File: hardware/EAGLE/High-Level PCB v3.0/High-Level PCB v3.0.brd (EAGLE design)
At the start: 100 x 80 mm, 58 parts, among them IC1 MCP2551, IC2 DS8921, IC3 DS8921, J1 Micro-SD, J2 Optical Mouse, J3 Gyro, J4 DB9 Plug, J5 CAN Output, J6 RaspπUart, U1 GPS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

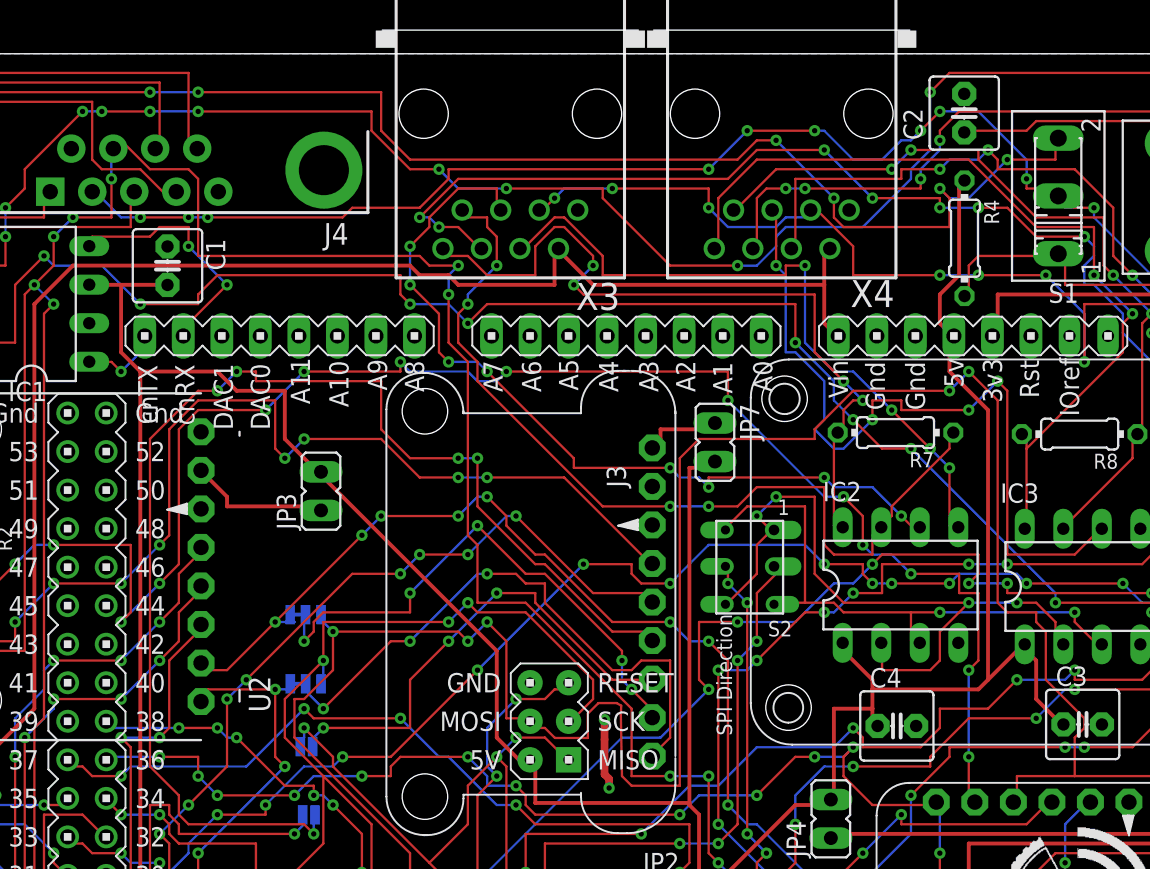
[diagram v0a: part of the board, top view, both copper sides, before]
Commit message: Fixed Click signal and made new gerbers
Click signals from the low level systems are now tied together.
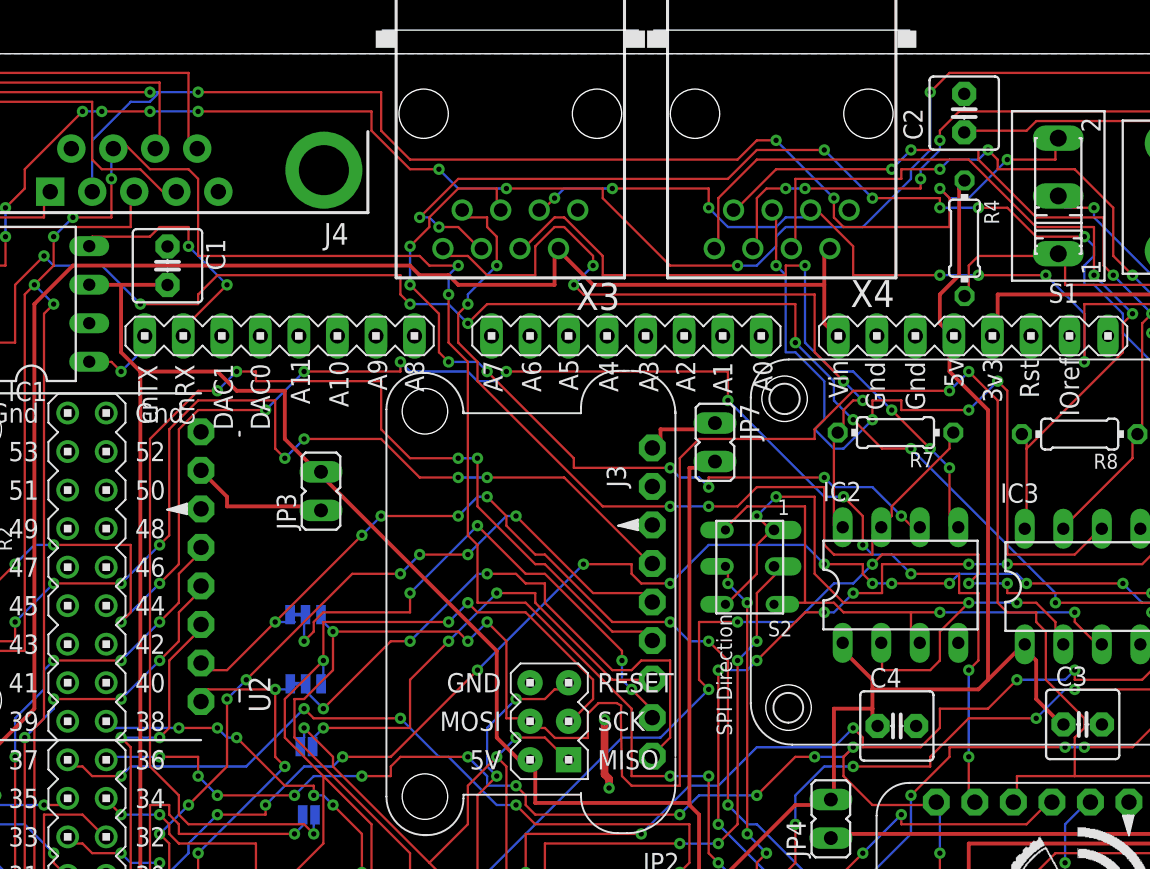
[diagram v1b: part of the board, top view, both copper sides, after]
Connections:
- removed net N$6: S1.3, X2.21
- new net CLICK_LL: J4.4, S1.3, X2.21
- net CLICK: no longer J4.4
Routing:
- net CLICK_LL: track 0.00 -> 166.7 mm, vias 0 -> 10
- net N$6: track 157.5 -> 0.00 mm, vias 10 -> 0
- net CLICK: track 164.8 -> 92.0 mm, vias 17 -> 8
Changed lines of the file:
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@@
 <via x="56.3" y="31.6" extent="1-16" drill="0.35"/>
 <via x="56" y="36.1" extent="1-16" drill="0.35"/>
-<wire x1="56" y1="32.5" x2="56" y2="34.8" width="0.508" layer="1"/>
-<wire x1="56" y1="34.8" x2="56" y2="36.1" width="0.508" layer="1"/>
+<wire x1="56" y1="32.5" x2="56" y2="36.1" width="0.508" layer="1"/>
 <wire x1="56.3" y1="31.6" x2="56.3" y2="32.2" width="0.508" layer="1"/>
 <wire x1="56.3" y1="32.2" x2="56" y2="32.5" width="0.508" layer="1"/>
@@
 <contactref element="S1" pad="2"/>
 <contactref element="U3" pad="17"/>
-<contactref element="J4" pad="4"/>
-<wire x1="83.82" y1="71.12" x2="85.725" y2="71.12" width="0.1524" layer="1"/>
-<wire x1="83.82" y1="71.755" x2="83.82" y2="71.12" width="0.1524" layer="1"/>
-<wire x1="83.82" y1="73.025" x2="83.82" y2="71.755" width="0.1524" layer="16"/>
-<wire x1="80.645" y1="76.2" x2="83.82" y2="73.025" width="0.1524" layer="16"/>
-<wire x1="78.105" y1="76.2" x2="80.645" y2="76.2" width="0.1524" layer="16"/>
-<wire x1="76.835" y1="74.93" x2="78.105" y2="76.2" width="0.1524" layer="1"/>
-<wire x1="76.2" y1="74.295" x2="76.835" y2="74.93" width="0.1524" layer="16"/>
-<wire x1="75.565" y1="74.295" x2="76.2" y2="74.295" width="0.1524" layer="16"/>
-<wire x1="74.295" y1="73.025" x2="75.565" y2="74.295" width="0.1524" layer="16"/>
-<wire x1="72.39" y1="73.025" x2="74.295" y2="73.025" width="0.1524" layer="16"/>
-<wire x1="70.485" y1="74.93" x2="72.39" y2="73.025" width="0.1524" layer="16"/>
-<wire x1="69.85" y1="74.93" x2="70.485" y2="74.93" width="0.1524" layer="16"/>
-<wire x1="65.405" y1="74.93" x2="69.85" y2="74.93" width="0.1524" layer="1"/>
-<wire x1="62.865" y1="72.39" x2="65.405" y2="74.93" width="0.1524" layer="16"/>
-<wire x1="45.72" y1="72.39" x2="62.865" y2="72.39" width="0.1524" layer="1"/>
-<wire x1="45.72" y1="71.755" x2="45.72" y2="72.39" width="0.1524" layer="1"/>
-<wire x1="43.815" y1="69.85" x2="45.72" y2="71.755" width="0.1524" layer="1"/>
-<wire x1="39.37" y1="69.85" x2="43.815" y2="69.85" width="0.1524" layer="1"/>
-<wire x1="38.735" y1="69.215" x2="39.37" y2="69.85" width="0.1524" layer="1"/>
-<wire x1="29.845" y1="69.215" x2="38.735" y2="69.215" width="0.1524" layer="1"/>
-<wire x1="28.575" y1="69.215" x2="29.845" y2="69.215" width="0.1524" layer="16"/>
-<wire x1="25.4" y1="69.215" x2="28.575" y2="69.215" width="0.1524" layer="1"/>
-<wire x1="24.13" y1="69.215" x2="25.4" y2="69.215" width="0.1524" layer="16"/>
-<wire x1="22.86" y1="70.485" x2="24.13" y2="69.215" width="0.1524" layer="16"/>
-<wire x1="85.725" y1="71.12" x2="85.91" y2="70.63" width="0.1524" layer="1"/>
-<wire x1="22.86" y1="70.485" x2="22.23" y2="70.91" width="0.1524" layer="16"/>
 <wire x1="64.77" y1="21.59" x2="63.5" y2="20.32" width="0.1524" layer="1"/>
 <wire x1="67.945" y1="21.59" x2="64.77" y2="21.59" width="0.1524" layer="16"/>
@@
 <wire x1="63.5" y1="20.32" x2="63.4" y2="19.86" width="0.1524" layer="1"/>
 <wire x1="86.36" y1="70.485" x2="85.91" y2="70.63" width="0.1524" layer="1"/>
-<via x="83.82" y="71.755" extent="1-16" drill="0.35"/>
-<via x="78.105" y="76.2" extent="1-16" drill="0.35"/>
-<via x="76.835" y="74.93" extent="1-16" drill="0.35"/>
-<via x="69.85" y="74.93" extent="1-16" drill="0.35"/>
-<via x="65.405" y="74.93" extent="1-16" drill="0.35"/>
-<via x="62.865" y="72.39" extent="1-16" drill="0.35"/>
-<via x="29.845" y="69.215" extent="1-16" drill="0.35"/>
-<via x="28.575" y="69.215" extent="1-16" drill="0.35"/>
-<via x="25.4" y="69.215" extent="1-16" drill="0.35"/>
 <via x="64.77" y="21.59" extent="1-16" drill="0.35"/>
 <via x="67.945" y="21.59" extent="1-16" drill="0.35"/>
@@
 <via x="18.415" y="64.77" extent="1-16" drill="0.35"/>
 </signal>
-<signal name="N$6">
+<signal name="CLICK_LL">
 <contactref element="S1" pad="3"/>
 <contactref element="X2" pad="21"/>
@@
 <wire x1="12.7" y1="77.47" x2="11.43" y2="76.2" width="0.1524" layer="1"/>
 <wire x1="26.035" y1="77.47" x2="12.7" y2="77.47" width="0.1524" layer="1"/>
-<wire x1="29.21" y1="77.47" x2="26.035" y2="77.47" width="0.1524" layer="16"/>
+<wire x1="29.21" y1="77.47" x2="26.67" y2="77.47" width="0.1524" layer="16"/>
+<wire x1="26.67" y1="77.47" x2="26.035" y2="77.47" width="0.1524" layer="16"/>
 <wire x1="41.275" y1="77.47" x2="29.21" y2="77.47" width="0.1524" layer="1"/>
 <wire x1="41.275" y1="74.93" x2="41.275" y2="77.47" width="0.1524" layer="1"/>
@@
 <via x="78.105" y="71.12" extent="1-16" drill="0.35"/>
 <via x="82.55" y="73.025" extent="1-16" drill="0.35"/>
+<contactref element="J4" pad="4"/>
+<wire x1="22.225" y1="74.295" x2="22.225" y2="71.12" width="0.1524" layer="16"/>
+<wire x1="24.765" y1="76.835" x2="22.225" y2="74.295" width="0.1524" layer="16"/>
+<wire x1="26.035" y1="76.835" x2="24.765" y2="76.835" width="0.1524" layer="16"/>
+<wire x1="26.67" y1="77.47" x2="26.035" y2="76.835" width="0.1524" layer="16"/>
+<wire x1="22.225" y1="71.12" x2="22.23" y2="70.91" width="0.1524" layer="16"/>
 </signal>
 <signal name="N$7">

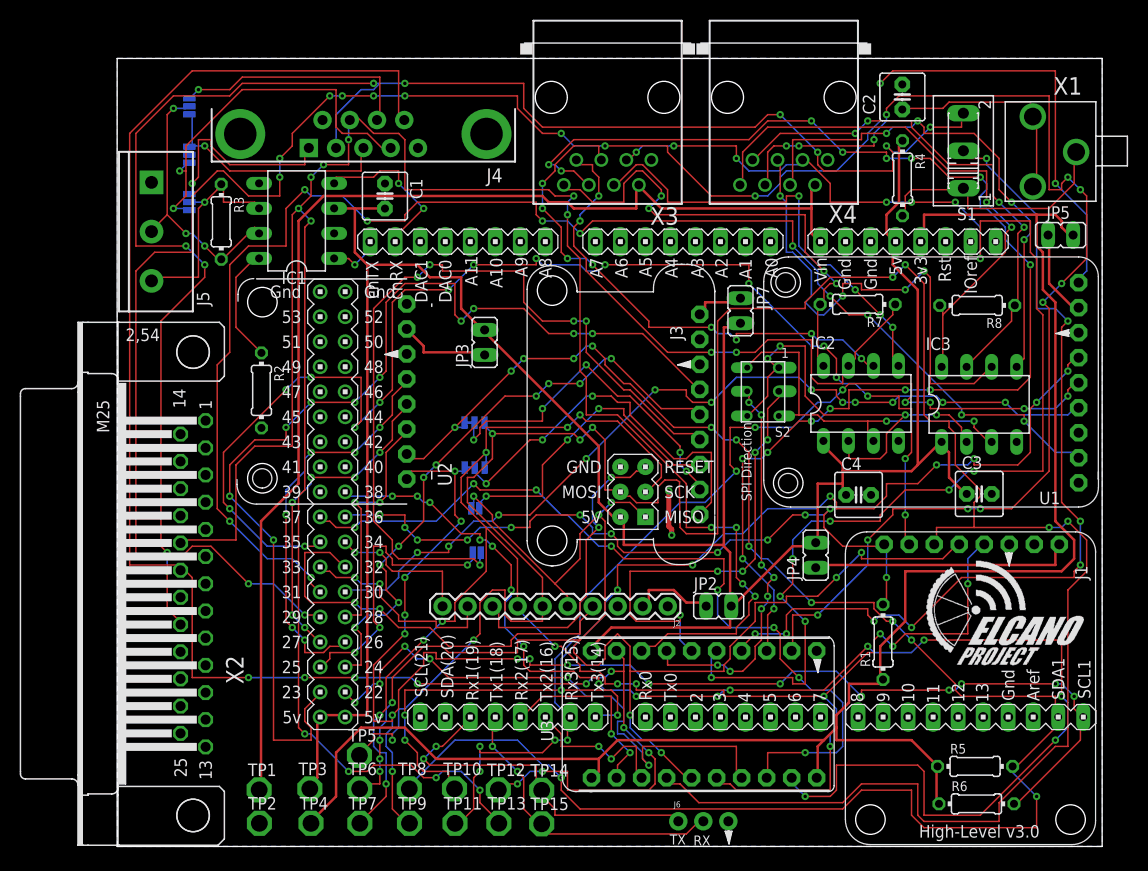
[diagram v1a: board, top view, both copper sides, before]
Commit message: Fixed SPST size and generated new Gerbers
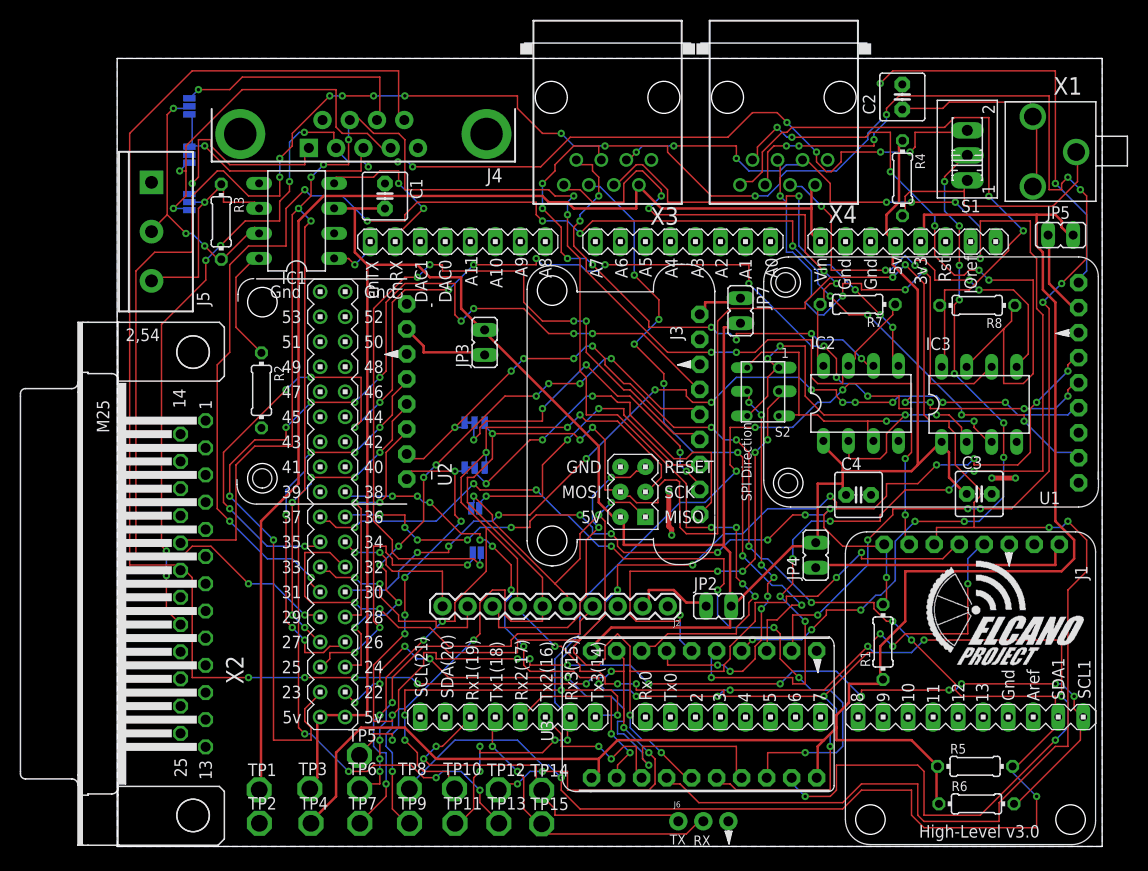
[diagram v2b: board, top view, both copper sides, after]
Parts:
- S1: device switch:255SB -> ELCano_Footprints:SP_ELSWITCH
- moved S1 0.89 mm to (86.3, 71.4)
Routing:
- net CS_C5_FRONT_5V: track 131.5 -> 64.8 mm, vias 16 -> 7
- net CLICK_LL: track 166.7 -> 138.0 mm, vias 10 -> 13
- net CLICK: track 92.0 -> 74.3 mm, vias 8 -> 12
- net MOSI-R: track 52.5 -> 69.0 mm, vias 4 -> 6
- net MISO-R: track 51.8 -> 41.7 mm, vias 4 -> 5
- net MOSI+R: track 56.1 -> 61.6 mm
- net GND: track 4.62 -> 7.02 mm, vias 2 -> 4
- net N$7: track 26.0 -> 26.8 mm
